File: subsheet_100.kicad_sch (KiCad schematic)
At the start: 21 parts, among them Q01 16MHz

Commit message: assign footprints to L01 and Q01
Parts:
- Q01: footprint (none) -> Crystal:Crystal_HC49-U_Horizontal
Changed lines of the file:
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@@
       (effects (font (size 1.27 1.27)) (justify left))
     )
-    (property "Footprint" "" (at 168.91 229.87 0)
+    (property "Footprint" "Crystal:Crystal_HC49-U_Horizontal" (at 168.91 229.87 0)
       (effects (font (size 1.27 1.27)) hide)
     )

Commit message: created and assigned footprints : keyboard and video connectors ; standard barrel-jack ; 6mm standard push button ; trimpot
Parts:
- S01: footprint (none) -> Potentiometer_THT:Potentiometer_ACP_CA9-V10_Vertical_Hole
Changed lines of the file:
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@@
       (effects (font (size 1.27 1.27)))
     )
-    (property "Footprint" "" (at 167.64 60.96 0)
+    (property "Footprint" "Potentiometer_THT:Potentiometer_ACP_CA9-V10_Vertical_Hole" (at 167.64 60.96 0)
       (effects (font (size 1.27 1.27)) hide)
     )

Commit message: fixed : S01 footprint
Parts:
- S01: footprint Potentiometer_THT:Potentiometer_ACP_CA9-V10_Vertical_Hole -> Button_Switch_THT:SW_PUSH_6mm
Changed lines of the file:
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@@
       (effects (font (size 1.27 1.27)))
     )
-    (property "Footprint" "Potentiometer_THT:Potentiometer_ACP_CA9-V10_Vertical_Hole" (at 167.64 60.96 0)
+    (property "Footprint" "Button_Switch_THT:SW_PUSH_6mm" (at 167.64 60.96 0)
       (effects (font (size 1.27 1.27)) hide)
     )

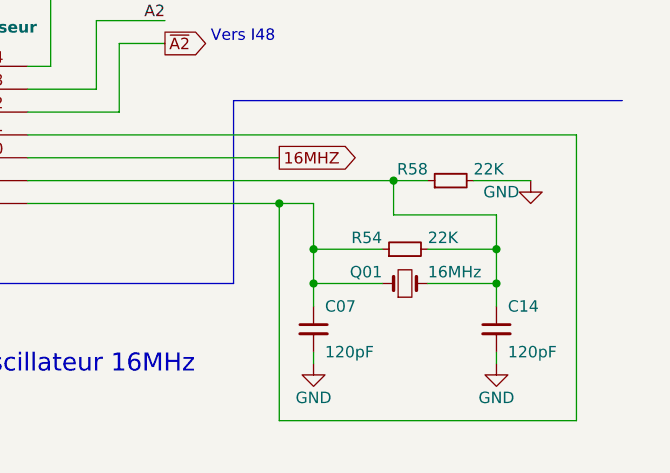
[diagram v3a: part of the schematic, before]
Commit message: placement : Cpu, gate array, I16, I21, Q01 and passives
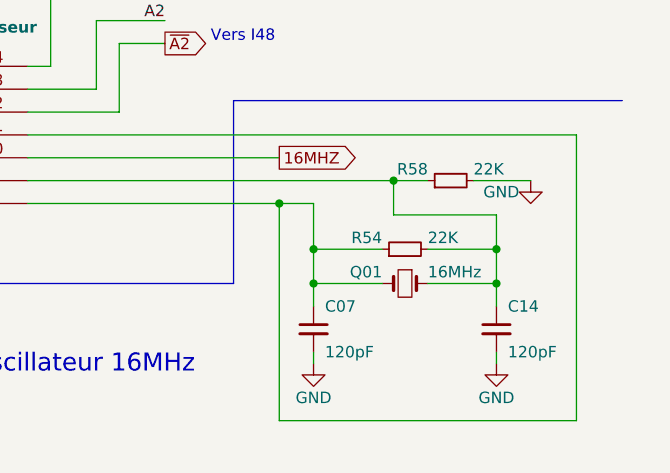
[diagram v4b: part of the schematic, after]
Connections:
- net at C07.1, I21.11 (5A), I21.8 (4Y)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: now also Q01.2; no longer Q01.1
- net at C14.1, I21.9 (4A), R54.2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: now also Q01.1; no longer Q01.2
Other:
- moved on the sheet: Q01
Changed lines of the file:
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@@
     )
   )
-  (symbol (lib_id "Device:Crystal_Small") (at 168.91 229.87 0) (unit 1)
+  (symbol (lib_id "Device:Crystal_Small") (at 168.91 229.87 180) (unit 1)
     (in_bom yes) (on_board yes) (dnp no)
     (property "Reference" "Q01" (at 166.37 228.6 0)
+      (effects (font (size 1.27 1.27)) (justify left))
+    )
+    (property "Value" "16MHz" (at 171.45 228.6 0)
       (effects (font (size 1.27 1.27)) (justify right))
     )
-    (property "Value" "16MHz" (at 171.45 228.6 0)
-      (effects (font (size 1.27 1.27)) (justify left))
-    )
     (property "Footprint" "Crystal:Crystal_HC49-U_Horizontal" (at 168.91 229.87 0)
